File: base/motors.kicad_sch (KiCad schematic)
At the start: 42 parts, among them IC1 TMC2209-LA-T, IC2 TMC2209-LA-T, IC3 TMC2209-LA-T, J10 receptable 4 way, J11 receptable 4 way, J12 receptable 4 way, J14 cable assembly, J6 heatsink_tmc, J7 heatsink_tmc, J8 heatsink_tmc

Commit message: send to fab
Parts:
- R7: value 10K -> 5.1K; farnell# 2826162 -> 1469937; manf# CRCW080510K0JNEAC -> CRCW08055K10FKEA; mouser# 71-CRCW080510K0JNEAC -> -71-CRCW0805-5.1K-E3
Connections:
- net +3.3V: no longer IC1.17 (VREF), IC2.17 (VREF), IC3.17 (VREF)
- no-connect marks 13 -> 16

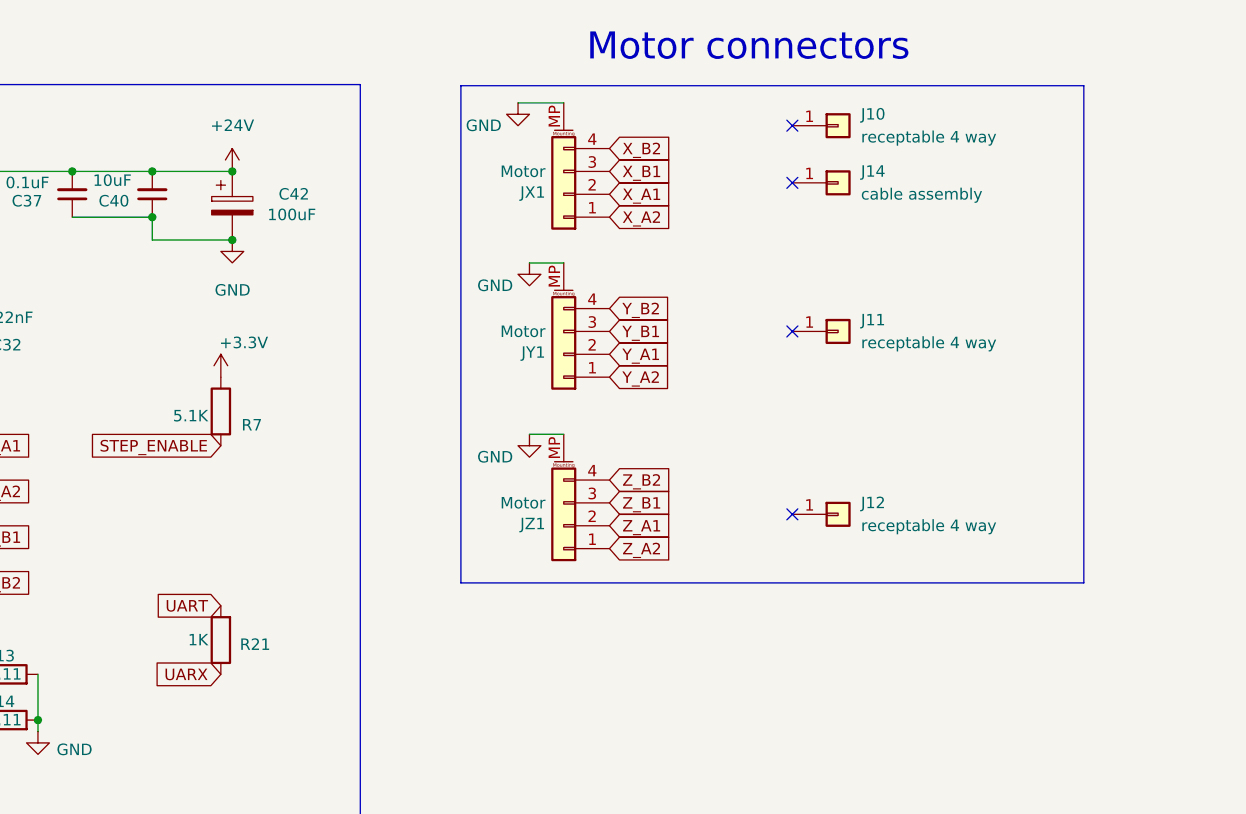
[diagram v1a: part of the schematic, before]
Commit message: fixed: uartx res to 5.1K, switch connection cross, camera connextor top side
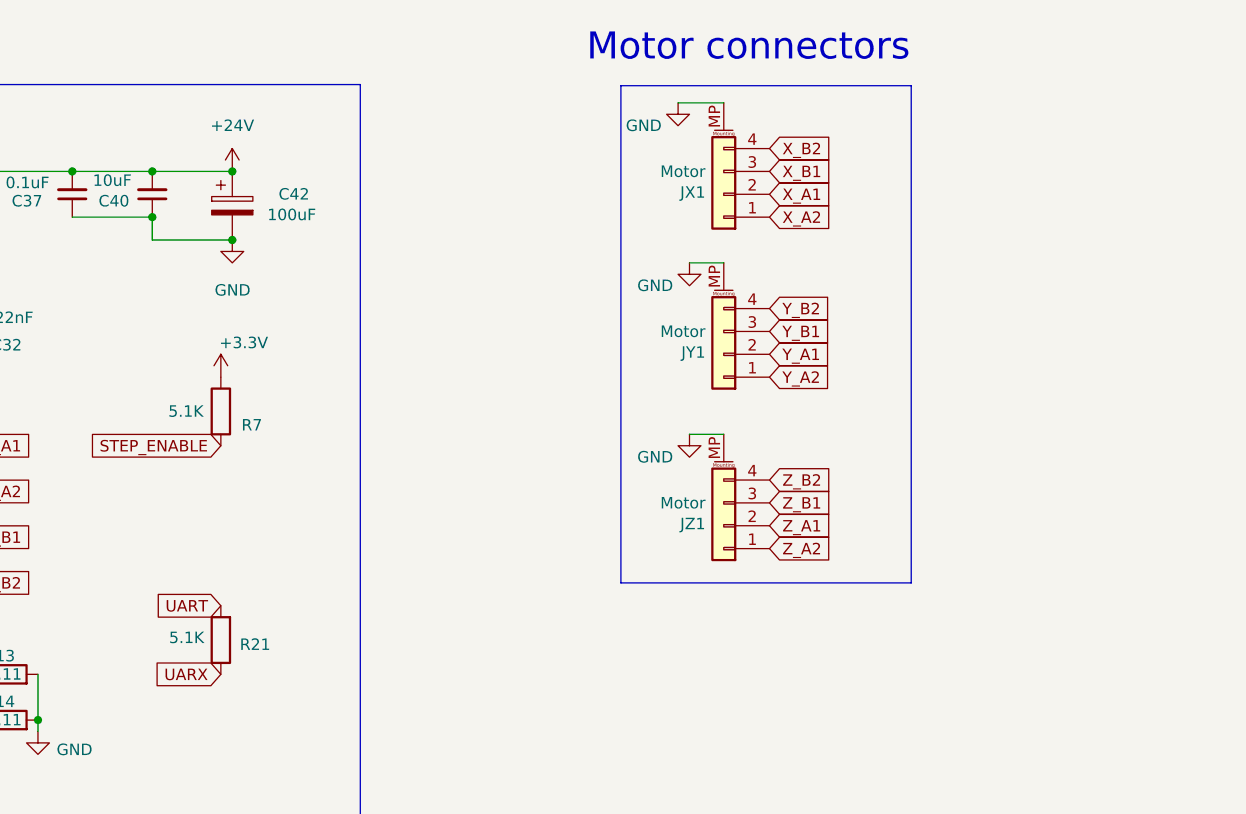
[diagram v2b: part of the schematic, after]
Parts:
- removed J10, J11, J12: receptable 4 way, symbol Connector_Generic:Conn_01x01
- removed J14: cable assembly, symbol Connector_Generic:Conn_01x01
- R21: value 1K -> 5.1K; footprint Resistor_SMD:R_0805_2012Metric_Pad1.20x1.40mm_HandSolder -> Resistor_SMD:R_0805_2012Metric; manf# CRCW08051K00FKEA -> CRCW08055K10FKEA; mouser# 71-CRCW0805-1.0K-E3 -> -71-CRCW0805-5.1K-E3
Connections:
- no-connect marks 16 -> 12
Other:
- moved on the sheet: JX1, JY1, JZ1
